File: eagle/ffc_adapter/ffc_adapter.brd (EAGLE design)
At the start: 48.5 x 9.3 mm, 10 parts, among them J1 FH12-6S-0.5SH(55), J2 FH12-6S-0.5SH(55), J3 FH12-6S-0.5SH(55), J4 FH12-6S-0.5SH(55), J5 FH12-6S-0.5SH(55)

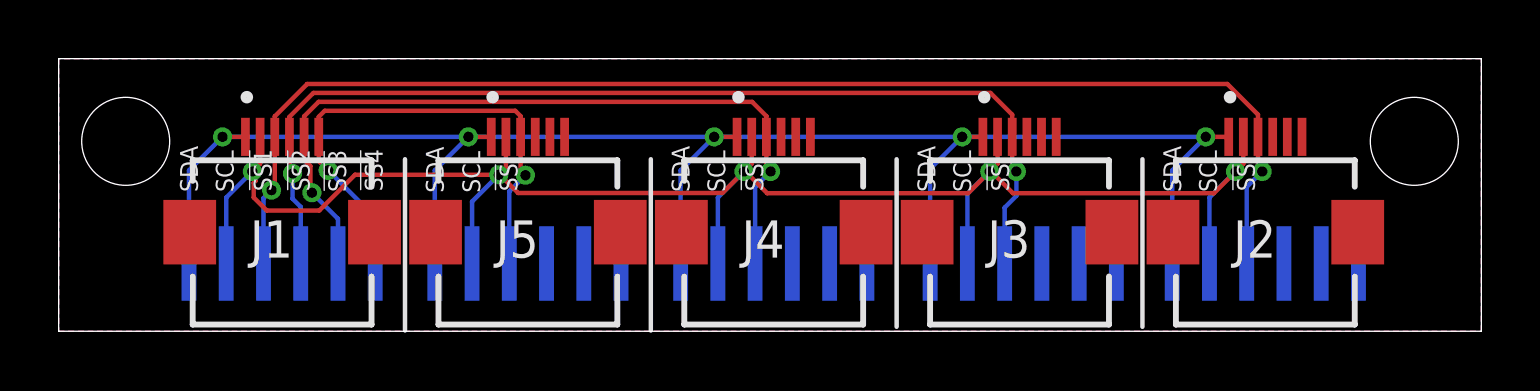
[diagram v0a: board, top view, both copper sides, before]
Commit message: Update the FFC adapter to use bottom contact connectors;
The previous design had the pin orders to match those in the connector
board. When using a forward direction cable (contacts on the same side
on both ends) and a top contact connector on both ends, the pin order
would get mirrored. Because the forward direction cable and the top
contact connectors are (supposedly?) the norm, it's probably better to
just reverse the pins on the adapter in order to be able to use the same
connectors and cables everywhere.
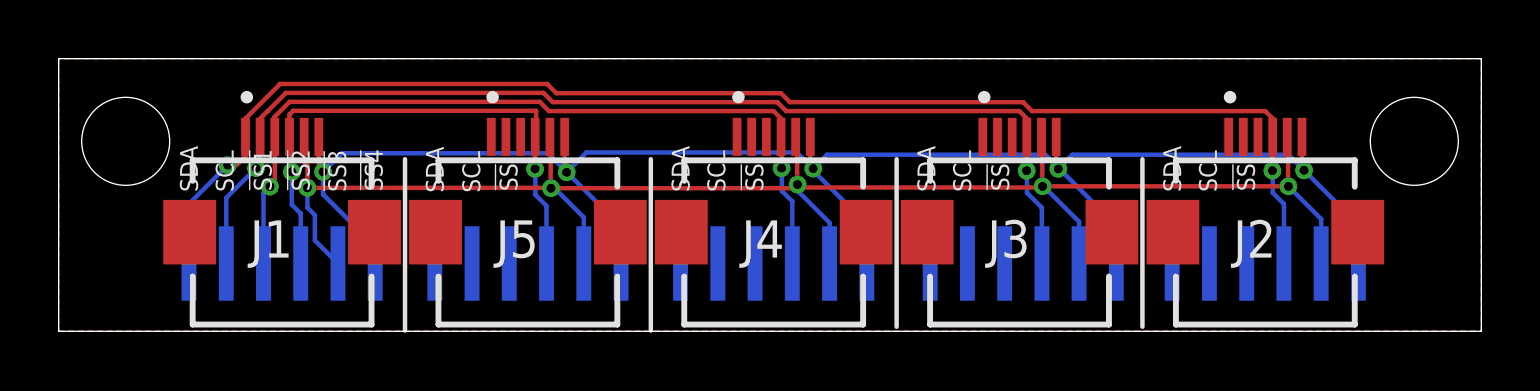
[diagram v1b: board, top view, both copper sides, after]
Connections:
- net !SS1: now also J1.4, J5.4, U$4.P$3, U$5.P$3; no longer J1.3, J2.3, U$1.P$4, U$4.P$4
- net !SS2: now also J1.3, J4.4, U$3.P$3, U$4.P$4; no longer J1.4, J3.3, U$2.P$4, U$4.P$3
- net !SS3: now also J1.2, J3.4, U$2.P$3, U$4.P$5; no longer J1.5, J4.3, U$3.P$4, U$4.P$2
- net !SS4: now also J1.1, J2.4, U$1.P$3, U$4.P$6; no longer J1.6, J5.3, U$4.P$1, U$5.P$4
- net SCL: now also J1.5, J2.5, J3.5, J4.5, J5.5, U$1.P$2, U$2.P$2, U$3.P$2, U$4.P$2, U$5.P$2; no longer J1.2, J2.2, J3.2, J4.2, J5.2, U$1.P$5, U$2.P$5, U$3.P$5, U$4.P$5, U$5.P$5
- net SDA: now also J1.6, J2.6, J3.6, J4.6, J5.6, U$1.P$1, U$2.P$1, U$3.P$1, U$4.P$1, U$5.P$1; no longer J1.1, J2.1, J3.1, J4.1, J5.1, U$1.P$6, U$2.P$6, U$3.P$6, U$4.P$6, U$5.P$6
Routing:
- net !SS4: track 18.2 -> 47.0 mm
- net !SS1: track 44.9 -> 19.1 mm
- net !SS3: track 27.0 -> 37.5 mm
- net !SS2: track 35.8 -> 28.0 mm
- net SCL: track 60.8 -> 57.7 mm
